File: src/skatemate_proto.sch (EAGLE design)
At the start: 101 parts, among them IC1 REG1117, Q1 IRF740, Q2 IRF740, Q3 IRF740, Q4 IRF740, Q5 IRF740, Q6 IRF740, U1 DRV8301DCAR

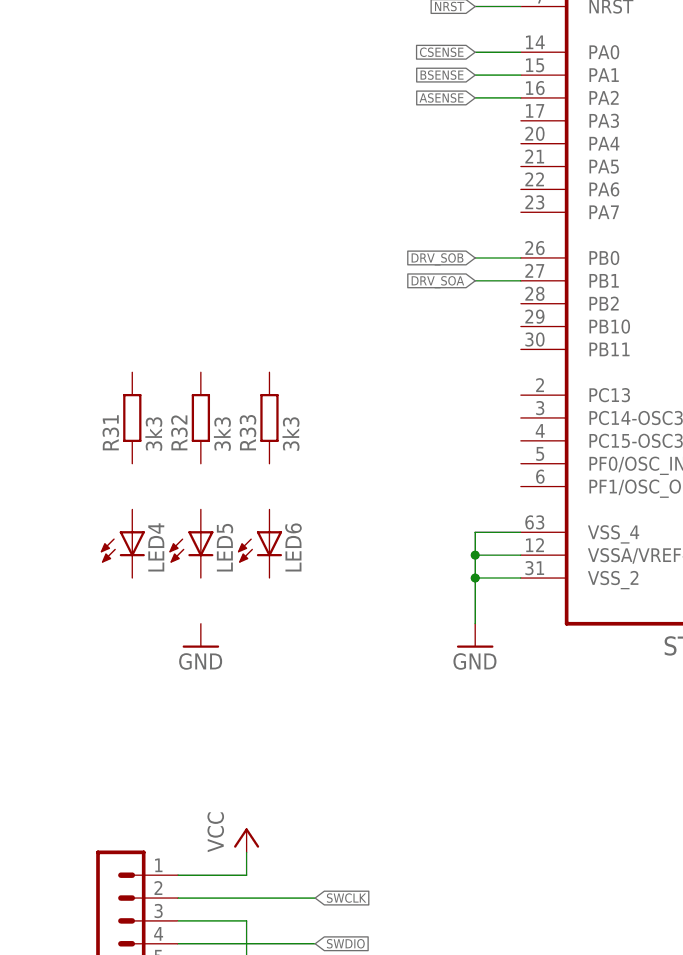
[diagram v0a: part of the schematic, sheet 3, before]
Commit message: Added LED and crystal
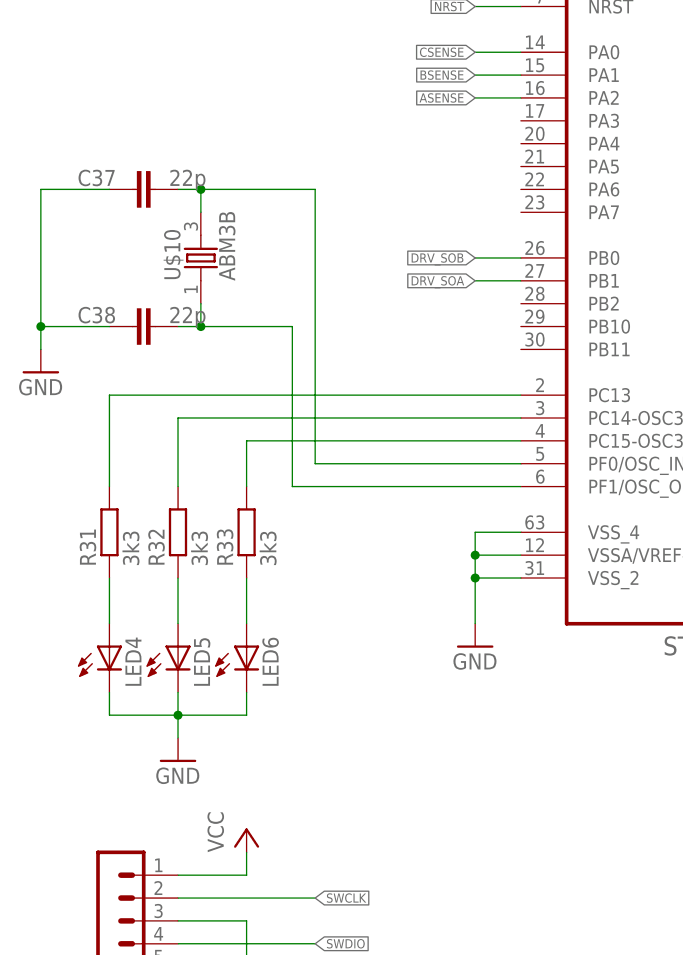
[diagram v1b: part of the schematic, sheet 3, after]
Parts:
- added C37, C38: 22p, skatemate:C-EUC0805
- added U$10: ABM3B, skatemate:ABM3B
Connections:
- new net N$28: R33.2, U$3G$1.PC15-OSC32_OUT
- new net N$29: R32.2, U$3G$1.PC14-OSC32_IN
- new net N$30: R31.2, U$3G$1.PC13
- new net N$31: LED4.A, R31.1
- new net N$32: LED5.A, R32.1
- new net N$33: LED6.A, R33.1
- new net N$35: C38.2, U$10.1, U$3G$1.PF1/OSC_OUT
- new net N$36: C37.2, U$10.2, U$3G$1.PF0/OSC_IN
- net GND: now also C37.1, C38.1, LED4.C, LED5.C, LED6.C
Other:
- moved on the sheet: LED4, LED5, LED6, R31, R32, R33
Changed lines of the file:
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@@
 <part name="R33" library="skatemate" deviceset="R-EU_" device="R0805" value="3k3"/>
 <part name="GND21" library="supply1" deviceset="GND" device=""/>
+<part name="U$10" library="skatemate" deviceset="ABM3B" device=""/>
+<part name="C37" library="skatemate" deviceset="C-EU" device="C0805" value="22p"/>
+<part name="C38" library="skatemate" deviceset="C-EU" device="C0805" value="22p"/>
+<part name="GND20" library="supply1" deviceset="GND" device=""/>
 </parts>
 <sheets>
@@
 <instance part="U$3" gate="G$1" x="78.74" y="104.14"/>
 <instance part="U$3" gate="G$2" x="198.12" y="104.14"/>
-<instance part="LED4" gate="G$1" x="12.7" y="71.12"/>
-<instance part="LED5" gate="G$1" x="20.32" y="71.12"/>
-<instance part="LED6" gate="G$1" x="27.94" y="71.12"/>
-<instance part="R31" gate="G$1" x="12.7" y="83.82" rot="R90"/>
-<instance part="R32" gate="G$1" x="20.32" y="83.82" rot="R90"/>
-<instance part="R33" gate="G$1" x="27.94" y="83.82" rot="R90"/>
-<instance part="GND21" gate="1" x="20.32" y="58.42"/>
+<instance part="LED4" gate="G$1" x="10.16" y="58.42"/>
+<instance part="LED5" gate="G$1" x="17.78" y="58.42"/>
+<instance part="LED6" gate="G$1" x="25.4" y="58.42"/>
+<instance part="R31" gate="G$1" x="10.16" y="71.12" rot="R90"/>
+<instance part="R32" gate="G$1" x="17.78" y="71.12" rot="R90"/>
+<instance part="R33" gate="G$1" x="25.4" y="71.12" rot="R90"/>
+<instance part="GND21" gate="1" x="17.78" y="45.72"/>
+<instance part="U$10" gate="G$1" x="20.32" y="101.6" rot="R90"/>
+<instance part="C37" gate="G$1" x="12.7" y="109.22" smashed="yes" rot="R90">
+<attribute name="NAME" x="6.604" y="109.601" size="1.778" layer="95"/>
+<attribute name="VALUE" x="16.764" y="109.601" size="1.778" layer="96"/>
+</instance>
+<instance part="C38" gate="G$1" x="12.7" y="93.98" smashed="yes" rot="R90">
+<attribute name="NAME" x="6.604" y="94.361" size="1.778" layer="95"/>
+<attribute name="VALUE" x="16.764" y="94.361" size="1.778" layer="96"/>
+</instance>
+<instance part="GND20" gate="1" x="2.54" y="88.9"/>
 </instances>
 <busses>
@@
 <junction x="147.32" y="137.16"/>
 </segment>
+<segment>
+<pinref part="LED4" gate="G$1" pin="C"/>
+<wire x1="10.16" y1="53.34" x2="10.16" y2="50.8" width="0.1524" layer="91"/>
+<pinref part="LED6" gate="G$1" pin="C"/>
+<wire x1="10.16" y1="50.8" x2="17.78" y2="50.8" width="0.1524" layer="91"/>
+<wire x1="17.78" y1="50.8" x2="25.4" y2="50.8" width="0.1524" layer="91"/>
+<wire x1="25.4" y1="50.8" x2="25.4" y2="53.34" width="0.1524" layer="91"/>
+<pinref part="LED5" gate="G$1" pin="C"/>
+<wire x1="17.78" y1="53.34" x2="17.78" y2="50.8" width="0.1524" layer="91"/>
+<junction x="17.78" y="50.8"/>
+<pinref part="GND21" gate="1" pin="GND"/>
+<wire x1="17.78" y1="50.8" x2="17.78" y2="48.26" width="0.1524" layer="91"/>
+</segment>
+<segment>
+<pinref part="GND20" gate="1" pin="GND"/>
+<wire x1="2.54" y1="91.44" x2="2.54" y2="93.98" width="0.1524" layer="91"/>
+<pinref part="C37" gate="G$1" pin="1"/>
+<wire x1="2.54" y1="93.98" x2="2.54" y2="109.22" width="0.1524" layer="91"/>
+<wire x1="2.54" y1="109.22" x2="10.16" y2="109.22" width="0.1524" layer="91"/>
+<pinref part="C38" gate="G$1" pin="1"/>
+<wire x1="10.16" y1="93.98" x2="2.54" y2="93.98" width="0.1524" layer="91"/>
+<junction x="2.54" y="93.98"/>
+</segment>
 </net>
 <net name="N$22" class="0">
@@
 </segment>
 </net>
+<net name="N$28" class="0">
+<segment>
+<pinref part="U$3" gate="G$1" pin="PC15-OSC32_OUT"/>
+<pinref part="R33" gate="G$1" pin="2"/>
+<wire x1="55.88" y1="81.28" x2="25.4" y2="81.28" width="0.1524" layer="91"/>
+<wire x1="25.4" y1="81.28" x2="25.4" y2="76.2" width="0.1524" layer="91"/>
+</segment>
+</net>
+<net name="N$29" class="0">
+<segment>
+<pinref part="R32" gate="G$1" pin="2"/>
+<wire x1="17.78" y1="76.2" x2="17.78" y2="83.82" width="0.1524" layer="91"/>
+<pinref part="U$3" gate="G$1" pin="PC14-OSC32_IN"/>
+<wire x1="17.78" y1="83.82" x2="55.88" y2="83.82" width="0.1524" layer="91"/>
+</segment>
+</net>
+<net name="N$30" class="0">
+<segment>
+<pinref part="U$3" gate="G$1" pin="PC13"/>
+<pinref part="R31" gate="G$1" pin="2"/>
+<wire x1="55.88" y1="86.36" x2="10.16" y2="86.36" width="0.1524" layer="91"/>
+<wire x1="10.16" y1="86.36" x2="10.16" y2="76.2" width="0.1524" layer="91"/>
+</segment>
+</net>
+<net name="N$31" class="0">
+<segment>
+<pinref part="R31" gate="G$1" pin="1"/>
+<pinref part="LED4" gate="G$1" pin="A"/>
+<wire x1="10.16" y1="66.04" x2="10.16" y2="60.96" width="0.1524" layer="91"/>
+</segment>
+</net>
+<net name="N$32" class="0">
+<segment>
+<pinref part="R32" gate="G$1" pin="1"/>
+<pinref part="LED5" gate="G$1" pin="A"/>
+<wire x1="17.78" y1="66.04" x2="17.78" y2="60.96" width="0.1524" layer="91"/>
+</segment>
+</net>
+<net name="N$33" class="0">
+<segment>
+<pinref part="R33" gate="G$1" pin="1"/>
+<pinref part="LED6" gate="G$1" pin="A"/>
+<wire x1="25.4" y1="66.04" x2="25.4" y2="60.96" width="0.1524" layer="91"/>
+</segment>
+</net>
+<net name="N$35" class="0">
+<segment>
+<pinref part="C38" gate="G$1" pin="2"/>
+<wire x1="17.78" y1="93.98" x2="20.32" y2="93.98" width="0.1524" layer="91"/>
+<wire x1="20.32" y1="93.98" x2="30.48" y2="93.98" width="0.1524" layer="91"/>
+<wire x1="30.48" y1="93.98" x2="30.48" y2="76.2" width="0.1524" layer="91"/>
+<pinref part="U$3" gate="G$1" pin="PF1/OSC_OUT"/>
+<wire x1="30.48" y1="76.2" x2="55.88" y2="76.2" width="0.1524" layer="91"/>
+<pinref part="U$10" gate="G$1" pin="1"/>
+<wire x1="20.32" y1="96.52" x2="20.32" y2="93.98" width="0.1524" layer="91"/>
+<junction x="20.32" y="93.98"/>
+</segment>
+</net>
+<net name="N$36" class="0">
+<segment>
+<pinref part="U$3" gate="G$1" pin="PF0/OSC_IN"/>
+<wire x1="55.88" y1="78.74" x2="33.02" y2="78.74" width="0.1524" layer="91"/>
+<wire x1="33.02" y1="78.74" x2="33.02" y2="109.22" width="0.1524" layer="91"/>
+<wire x1="33.02" y1="109.22" x2="20.32" y2="109.22" width="0.1524" layer="91"/>
+<pinref part="C37" gate="G$1" pin="2"/>
+<pinref part="U$10" gate="G$1" pin="2"/>
+<wire x1="20.32" y1="109.22" x2="17.78" y2="109.22" width="0.1524" layer="91"/>
+<wire x1="20.32" y1="109.22" x2="20.32" y2="106.68" width="0.1524" layer="91"/>
+<junction x="20.32" y="109.22"/>
+</segment>
+</net>
